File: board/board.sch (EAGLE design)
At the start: 110 parts, among them IC1 STM32F05XC, IC2 MCP6N11-10, IC3 MCP45X1, IC4 LD117ADT33TR, IC5 FT230XS, IC6 MCP6002, IC7 LIS331, M1 MOSFET-NCHANNELFDD8580, M2 MOSFET-NCHANNELFDD8580, M3 MOSFET-NCHANNELFDD8580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

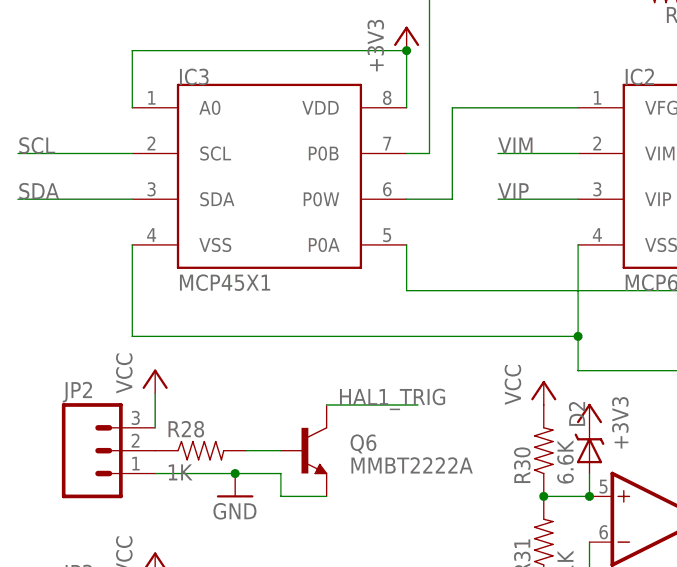
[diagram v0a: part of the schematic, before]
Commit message: Adding Nil RTOS, changed value of digital pot to proper part name.
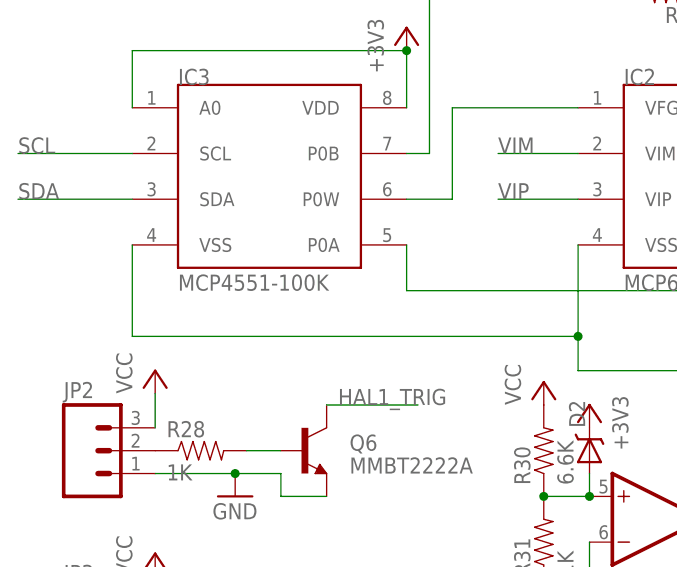
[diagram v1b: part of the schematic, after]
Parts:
- IC3: value MCP45X1 -> MCP4551-100K
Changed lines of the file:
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@@
 <part name="IC1" library="misc" deviceset="STM32F05XC" device=""/>
 <part name="IC2" library="misc" deviceset="MCP6N11" device="" value="MCP6N11-10"/>
-<part name="IC3" library="misc" deviceset="MCP45X1" device=""/>
+<part name="IC3" library="misc" deviceset="MCP45X1" device="" value="MCP4551-100K"/>
 <part name="IC4" library="v-reg" deviceset="LD117A?*" device="DT" technology="33TR"/>
 <part name="GND1" library="supply1" deviceset="GND" device=""/>

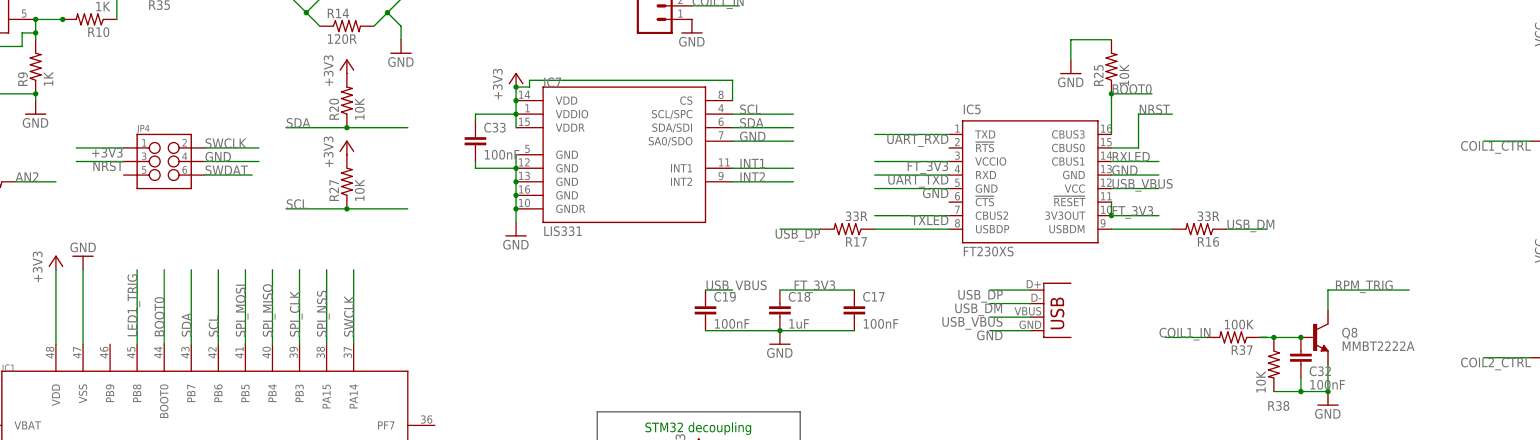
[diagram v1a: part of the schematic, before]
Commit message: Adding output for external fuel/igntion controller.
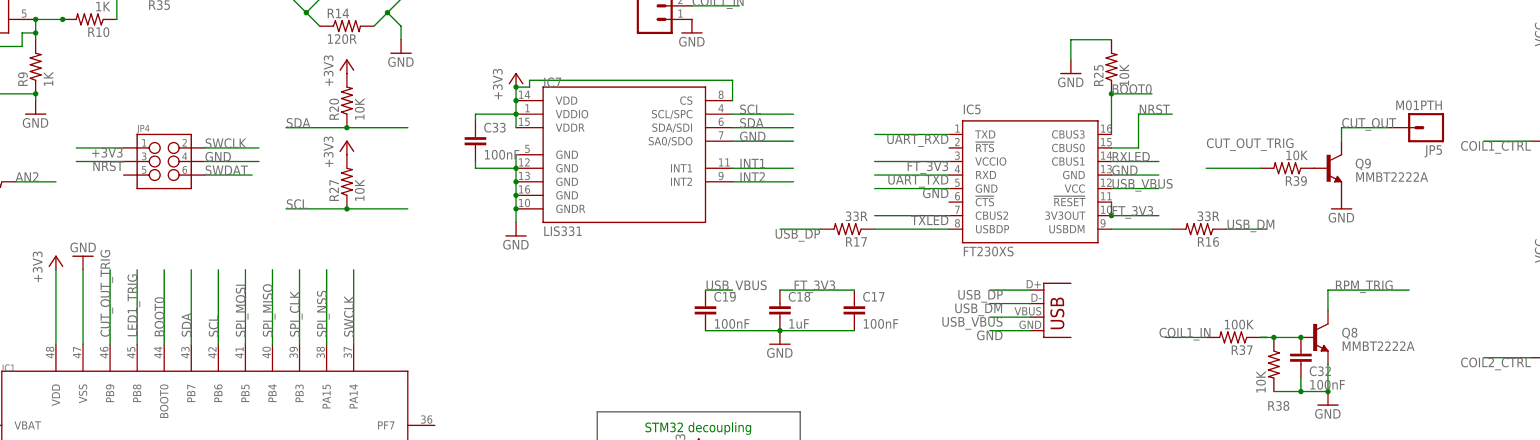
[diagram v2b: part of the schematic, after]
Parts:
- added JP5: M01PTH, SparkFun-Connectors:M01PTH
- added Q9: MMBT2222A, SparkFun-DiscreteSemi:TRANSISTOR_NPNMMBT2222A
- added R39: 10K, SparkFun-Resistors:RESISTOR0603-RES
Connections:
- new net CUT_OUT: JP5.1, Q9.C
- new net CUT_OUT_TRIG: IC1.PB9@46, R39.2
- new net N$37: Q9.B, R39.1
- net GND: now also Q9.E
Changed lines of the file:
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@@
 <grid distance="0.05" unitdist="inch" unit="inch" style="lines" multiple="1" display="yes" altdistance="0.005" altunitdist="inch" altunit="inch"/>
 <layers>
-<layer number="1" name="Top" color="4" fill="1" visible="no" active="no"/>
-<layer number="2" name="Route2" color="1" fill="3" visible="no" active="no"/>
-<layer number="3" name="Route3" color="4" fill="3" visible="no" active="no"/>
-<layer number="4" name="Route4" color="1" fill="4" visible="no" active="no"/>
-<layer number="5" name="Route5" color="4" fill="4" visible="no" active="no"/>
-<layer number="6" name="Route6" color="1" fill="8" visible="no" active="no"/>
-<layer number="7" name="Route7" color="4" fill="8" visible="no" active="no"/>
-<layer number="8" name="Route8" color="1" fill="2" visible="no" active="no"/>
-<layer number="9" name="Route9" color="4" fill="2" visible="no" active="no"/>
-<layer number="10" name="Route10" color="1" fill="7" visible="no" active="no"/>
-<layer number="11" name="Route11" color="4" fill="7" visible="no" active="no"/>
-<layer number="12" name="Route12" color="1" fill="5" visible="no" active="no"/>
-<layer number="13" name="Route13" color="4" fill="5" visible="no" active="no"/>
-<layer number="14" name="Route14" color="1" fill="6" visible="no" active="no"/>
-<layer number="15" name="Route15" color="4" fill="6" visible="no" active="no"/>
-<layer number="16" name="Bottom" color="1" fill="1" visible="no" active="no"/>
-<layer number="17" name="Pads" color="2" fill="1" visible="no" active="no"/>
-<layer number="18" name="Vias" color="2" fill="1" visible="no" active="no"/>
-<layer number="19" name="Unrouted" color="6" fill="1" visible="no" active="no"/>
-<layer number="20" name="Dimension" color="15" fill="1" visible="no" active="no"/>
-<layer number="21" name="tPlace" color="16" fill="1" visible="no" active="no"/>
-<layer number="22" name="bPlace" color="14" fill="1" visible="no" active="no"/>
-<layer number="23" name="tOrigins" color="15" fill="1" visible="no" active="no"/>
-<layer number="24" name="bOrigins" color="15" fill="1" visible="no" active="no"/>
-<layer number="25" name="tNames" color="7" fill="1" visible="no" active="no"/>
-<layer number="26" name="bNames" color="7" fill="1" visible="no" active="no"/>
-<layer number="27" name="tValues" color="7" fill="1" visible="no" active="no"/>
-<layer number="28" name="bValues" color="7" fill="1" visible="no" active="no"/>
+<layer number="1" name="Top" color="4" fill="1" visible="yes" active="no"/>
+<layer number="2" name="Route2" color="1" fill="3" visible="yes" active="no"/>
+<layer number="3" name="Route3" color="4" fill="3" visible="yes" active="no"/>
+<layer number="4" name="Route4" color="1" fill="4" visible="yes" active="no"/>
+<layer number="5" name="Route5" color="4" fill="4" visible="yes" active="no"/>
+<layer number="6" name="Route6" color="1" fill="8" visible="yes" active="no"/>
+<layer number="7" name="Route7" color="4" fill="8" visible="yes" active="no"/>
+<layer number="8" name="Route8" color="1" fill="2" visible="yes" active="no"/>
+<layer number="9" name="Route9" color="4" fill="2" visible="yes" active="no"/>
+<layer number="10" name="Route10" color="1" fill="7" visible="yes" active="no"/>
+<layer number="11" name="Route11" color="4" fill="7" visible="yes" active="no"/>
+<layer number="12" name="Route12" color="1" fill="5" visible="yes" active="no"/>
+<layer number="13" name="Route13" color="4" fill="5" visible="yes" active="no"/>
+<layer number="14" name="Route14" color="1" fill="6" visible="yes" active="no"/>
+<layer number="15" name="Route15" color="4" fill="6" visible="yes" active="no"/>
+<layer number="16" name="Bottom" color="1" fill="1" visible="yes" active="no"/>
+<layer number="17" name="Pads" color="2" fill="1" visible="yes" active="no"/>
+<layer number="18" name="Vias" color="2" fill="1" visible="yes" active="no"/>
+<layer number="19" name="Unrouted" color="6" fill="1" visible="yes" active="no"/>
+<layer number="20" name="Dimension" color="15" fill="1" visible="yes" active="no"/>
+<layer number="21" name="tPlace" color="16" fill="1" visible="yes" active="no"/>
+<layer number="22" name="bPlace" color="14" fill="1" visible="yes" active="no"/>
+<layer number="23" name="tOrigins" color="15" fill="1" visible="yes" active="no"/>
+<layer number="24" name="bOrigins" color="15" fill="1" visible="yes" active="no"/>
+<layer number="25" name="tNames" color="7" fill="1" visible="yes" active="no"/>
+<layer number="26" name="bNames" color="7" fill="1" visible="yes" active="no"/>
+<layer number="27" name="tValues" color="7" fill="1" visible="yes" active="no"/>
+<layer number="28" name="bValues" color="7" fill="1" visible="yes" active="no"/>
 <layer number="29" name="tStop" color="7" fill="3" visible="no" active="no"/>
 <layer number="30" name="bStop" color="7" fill="6" visible="no" active="no"/>
@@
 <layer number="35" name="tGlue" color="7" fill="4" visible="no" active="no"/>
 <layer number="36" name="bGlue" color="7" fill="5" visible="no" active="no"/>
-<layer number="37" name="tTest" color="7" fill="1" visible="no" active="no"/>
-<layer number="38" name="bTest" color="7" fill="1" visible="no" active="no"/>
+<layer number="37" name="tTest" color="7" fill="1" visible="yes" active="no"/>
+<layer number="38" name="bTest" color="7" fill="1" visible="yes" active="no"/>
 <layer number="39" name="tKeepout" color="4" fill="11" visible="no" active="no"/>
 <layer number="40" name="bKeepout" color="1" fill="11" visible="no" active="no"/>
@@
 <layer number="44" name="Drills" color="7" fill="1" visible="no" active="no"/>
 <layer number="45" name="Holes" color="7" fill="1" visible="no" active="no"/>
-<layer number="46" name="Milling" color="3" fill="1" visible="no" active="no"/>
-<layer number="47" name="Measures" color="7" fill="1" visible="no" active="no"/>
-<layer number="48" name="Document" color="7" fill="1" visible="no" active="no"/>
-<layer number="49" name="Reference" color="7" fill="1" visible="no" active="no"/>
-<layer number="50" name="dxf" color="7" fill="1" visible="no" active="no"/>
-<layer number="51" name="tDocu" color="6" fill="1" visible="no" active="no"/>
-<layer number="52" name="bDocu" color="7" fill="1" visible="no" active="no"/>
-<layer number="53" name="tGND_GNDA" color="7" fill="9" visible="no" active="no"/>
-<layer number="54" name="bGND_GNDA" color="1" fill="9" visible="no" active="no"/>
-<layer number="56" name="wert" color="7" fill="1" visible="no" active="no"/>
+<layer number="46" name="Milling" color="3" fill="1" visible="yes" active="no"/>
+<layer number="47" name="Measures" color="7" fill="1" visible="yes" active="no"/>
+<layer number="48" name="Document" color="7" fill="1" visible="yes" active="no"/>
+<layer number="49" name="Reference" color="7" fill="1" visible="yes" active="no"/>
+<layer number="50" name="dxf" color="7" fill="1" visible="yes" active="no"/>
+<layer number="51" name="tDocu" color="6" fill="1" visible="yes" active="no"/>
+<layer number="52" name="bDocu" color="7" fill="1" visible="yes" active="no"/>
+<layer number="53" name="tGND_GNDA" color="7" fill="9" visible="yes" active="no"/>
+<layer number="54" name="bGND_GNDA" color="1" fill="9" visible="yes" active="no"/>
+<layer number="56" name="wert" color="7" fill="1" visible="yes" active="no"/>
 <layer number="91" name="Nets" color="2" fill="1" visible="yes" active="yes"/>
 <layer number="92" name="Busses" color="1" fill="1" visible="yes" active="yes"/>
@@
 <part name="C33" library="SparkFun-Capacitors" deviceset="CAP" device="0603-CAP" value="100nF"/>
 <part name="C34" library="SparkFun-Passives" deviceset="CAP" device="0603-CAP" value="4.7uF"/>
+<part name="Q9" library="SparkFun-DiscreteSemi" deviceset="TRANSISTOR_NPN" device="MMBT2222A" value="MMBT2222A"/>
+<part name="GND38" library="supply1" deviceset="GND" device=""/>
+<part name="R39" library="SparkFun-Resistors" deviceset="RESISTOR" device="0603-RES" value="10K"/>
+<part name="JP5" library="SparkFun-Connectors" deviceset="M01" device="PTH" value="M01PTH"/>
 </parts>
 <sheets>
@@
 <instance part="C33" gate="G$1" x="162.56" y="148.59"/>
 <instance part="C34" gate="G$1" x="45.72" y="11.43"/>
+<instance part="Q9" gate="G$1" x="322.58" y="144.78"/>
+<instance part="GND38" gate="1" x="325.12" y="137.16"/>
+<instance part="R39" gate="G$1" x="314.96" y="144.78" rot="R180"/>
+<instance part="JP5" gate="G$1" x="341.63" y="152.4" rot="R180"/>
 </instances>
 <busses>
@@
 <label x="212.09" y="149.86" size="1.778" layer="95"/>
 </segment>
+<segment>
+<pinref part="Q9" gate="G$1" pin="E"/>
+<pinref part="GND38" gate="1" pin="GND"/>
+</segment>
 </net>
 <net name="+3V3" class="0">
@@
 </segment>
 </net>
+<net name="CUT_OUT_TRIG" class="0">
+<segment>
+<pinref part="IC1" gate="G$1" pin="PB9@46"/>
+<wire x1="93.98" y1="111.76" x2="93.98" y2="125.73" width="0.1524" layer="91"/>
+<label x="93.98" y="113.03" size="1.778" layer="95" rot="R90"/>
+</segment>
+<segment>
+<pinref part="R39" gate="G$1" pin="2"/>
+<wire x1="309.88" y1="144.78" x2="299.72" y2="144.78" width="0.1524" layer="91"/>
+<label x="299.72" y="148.59" size="1.778" layer="95"/>
+</segment>
+</net>
+<net name="N$37" class="0">
+<segment>
+<pinref part="Q9" gate="G$1" pin="B"/>
+<pinref part="R39" gate="G$1" pin="1"/>
+</segment>
+</net>
+<net name="CUT_OUT" class="0">
+<segment>
+<pinref part="Q9" gate="G$1" pin="C"/>
+<wire x1="325.12" y1="149.86" x2="325.12" y2="152.4" width="0.1524" layer="91"/>
+<wire x1="325.12" y1="152.4" x2="334.01" y2="152.4" width="0.1524" layer="91"/>
+<label x="325.12" y="152.4" size="1.778" layer="95"/>
+<pinref part="JP5" gate="G$1" pin="1"/>
+</segment>
+</net>

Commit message: Changed connectors
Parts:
- removed R12: 120R, SparkFun-Resistors:RESISTOR0603-RES
- removed X1: BU-SMA-G, con-coax:BU-SMA-G
- added JP8: (no value), SparkFun-Connectors:M03PTH
- JP2, JP3: device SparkFun-Connectors:M03JST-PTH -> SparkFun-Connectors:M03PTH
- JP7: device SparkFun-Connectors:M04JST-PTH -> SparkFun-Connectors:M04PTH
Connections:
- net +3V3: now also JP8.1; no longer R12.1
- net GND: now also JP8.3; no longer X1G1.GND
- net VIP: now also JP8.2; no longer R12.2, X1G1.1
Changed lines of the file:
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@@
 <part name="+3V4" library="supply1" deviceset="+3V3" device=""/>
 <part name="R11" library="SparkFun-Resistors" deviceset="RESISTOR" device="0603-RES" value="100K"/>
-<part name="R12" library="SparkFun-Resistors" deviceset="RESISTOR" device="0603-RES" value="120R"/>
 <part name="R13" library="SparkFun-Resistors" deviceset="RESISTOR" device="0603-RES" value="120R"/>
 <part name="R14" library="SparkFun-Resistors" deviceset="RESISTOR" device="0603-RES" value="120R"/>
-<part name="X1" library="con-coax" deviceset="BU-SMA-G" device=""/>
 <part name="+3V2" library="supply1" deviceset="+3V3" device=""/>
 <part name="GND7" library="supply1" deviceset="GND" device=""/>
@@
 <part name="R23" library="SparkFun-Resistors" deviceset="RESISTOR" device="0603-RES" value="1K"/>
 <part name="R24" library="SparkFun-Resistors" deviceset="RESISTOR" device="0603-RES" value="1K"/>
-<part name="JP3" library="SparkFun-Connectors" deviceset="M03" device="JST-PTH"/>
+<part name="JP3" library="SparkFun-Connectors" deviceset="M03" device="PTH"/>
 <part name="GND27" library="supply1" deviceset="GND" device=""/>
 <part name="Q5" library="SparkFun-DiscreteSemi" deviceset="TRANSISTOR_NPN" device="MMBT2222A" value="MMBT2222A">
@@
 <part name="P+7" library="supply1" deviceset="VCC" device=""/>
 <part name="R26" library="SparkFun-Resistors" deviceset="RESISTOR" device="0603-RES" value="1K"/>
-<part name="JP2" library="SparkFun-Connectors" deviceset="M03" device="JST-PTH"/>
+<part name="JP2" library="SparkFun-Connectors" deviceset="M03" device="PTH"/>
 <part name="GND26" library="supply1" deviceset="GND" device=""/>
 <part name="Q6" library="SparkFun-DiscreteSemi" deviceset="TRANSISTOR_NPN" device="MMBT2222A" value="MMBT2222A">
@@
 <part name="JP6" library="SparkFun-Connectors" deviceset="M06" device="3.5MM-6"/>
 <part name="GND31" library="supply1" deviceset="GND" device=""/>
-<part name="JP7" library="SparkFun-Connectors" deviceset="M04" device="JST-PTH"/>
+<part name="JP7" library="SparkFun-Connectors" deviceset="M04" device="PTH"/>
 <part name="Q7" library="SparkFun-DiscreteSemi" deviceset="TRANSISTOR_NPN" device="MMBT2222A" value="MMBT2222A">
 <attribute name="VALUE" value="MMBT2222A"/>
@@
 <part name="R39" library="SparkFun-Resistors" deviceset="RESISTOR" device="0603-RES" value="10K"/>
 <part name="JP5" library="SparkFun-Connectors" deviceset="M01" device="PTH" value="M01PTH"/>
+<part name="JP8" library="SparkFun-Connectors" deviceset="M03" device="PTH"/>
 </parts>
 <sheets>
@@
 <instance part="+3V4" gate="G$1" x="30.48" y="196.85"/>
 <instance part="R11" gate="G$1" x="59.69" y="200.66" rot="R180"/>
-<instance part="R12" gate="G$1" x="138.43" y="191.77"/>
 <instance part="R13" gate="G$1" x="128.27" y="181.61" rot="R270"/>
 <instance part="R14" gate="G$1" x="138.43" y="171.45"/>
-<instance part="X1" gate="G1" x="151.13" y="182.88" smashed="yes" rot="MR0">
-<attribute name="VALUE" x="154.94" y="177.8" size="1.778" layer="96" rot="MR90"/>
-<attribute name="NAME" x="153.67" y="186.182" size="1.778" layer="95" rot="MR0"/>
-</instance>
 <instance part="+3V2" gate="G$1" x="128.27" y="196.85"/>
 <instance part="GND7" gate="1" x="148.59" y="166.37"/>
@@
 <instance part="R39" gate="G$1" x="314.96" y="144.78" rot="R180"/>
 <instance part="JP5" gate="G$1" x="341.63" y="152.4" rot="R180"/>
+<instance part="JP8" gate="G$1" x="156.21" y="189.23" rot="R180"/>
 </instances>
 <busses>
@@
 <wire x1="146.05" y1="173.99" x2="148.59" y2="171.45" width="0.1524" layer="91"/>
 <junction x="146.05" y="173.99"/>
-<pinref part="X1" gate="G1" pin="GND"/>
 <wire x1="148.59" y1="180.34" x2="148.59" y2="176.53" width="0.1524" layer="91"/>
+<pinref part="JP8" gate="G$1" pin="3"/>
+<wire x1="148.59" y1="186.69" x2="148.59" y2="180.34" width="0.1524" layer="91"/>
 </segment>
 <segment>
@@
 </segment>
 <segment>
-<pinref part="R12" gate="G$1" pin="1"/>
 <pinref part="R13" gate="G$1" pin="1"/>
 <wire x1="128.27" y1="191.77" x2="128.27" y2="194.31" width="0.1524" layer="91"/>
@@
 <junction x="130.81" y="189.23"/>
 <pinref part="+3V2" gate="G$1" pin="+3V3"/>
+<pinref part="JP8" gate="G$1" pin="1"/>
+<wire x1="133.35" y1="191.77" x2="148.59" y2="191.77" width="0.1524" layer="91"/>
 </segment>
 <segment>
@@
 </segment>
 <segment>
-<pinref part="R12" gate="G$1" pin="2"/>
 <label x="140.97" y="185.42" size="1.778" layer="95" rot="R180"/>
-<wire x1="143.51" y1="191.77" x2="146.05" y2="189.23" width="0.1524" layer="91"/>
-<junction x="146.05" y="189.23"/>
-<wire x1="146.05" y1="189.23" x2="148.59" y2="186.69" width="0.1524" layer="91"/>
-<pinref part="X1" gate="G1" pin="1"/>
-<wire x1="148.59" y1="186.69" x2="148.59" y2="182.88" width="0.1524" layer="91"/>
 <wire x1="146.05" y1="189.23" x2="140.97" y2="184.15" width="0.1524" layer="91"/>
-</segment>
-</net>
+<pinref part="JP8" gate="G$1" pin="2"/>
+<wire x1="148.59" y1="189.23" x2="146.05" y2="189.23" width="0.1524" layer="91"/>
+</segment>
+</net>
